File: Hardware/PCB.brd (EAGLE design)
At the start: 46 x 35 mm, 105 parts, among them IC1 DRV2605YZFR_DRV2605YZFR, IC2 BQ25180YBGR_BQ25180YBGR, IC3 BMA423_BMA423, IC9 RT6160AWSC_RT6160AWSC, J1 503480-2400_503480-2400, J2 TC2030-IDC_TC2030-IDC, J4 KH-TYPE-C-16P_KH-TYPE-C-16P, Q3 ESP32_C6_LIBRARY_6_SI1308EDL-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, U1 NORDIC_NRF_4_NRF52840_QF, U3 ESP32_C6_LIBRARY_MAX17048G+T10, X2 32.768kHz

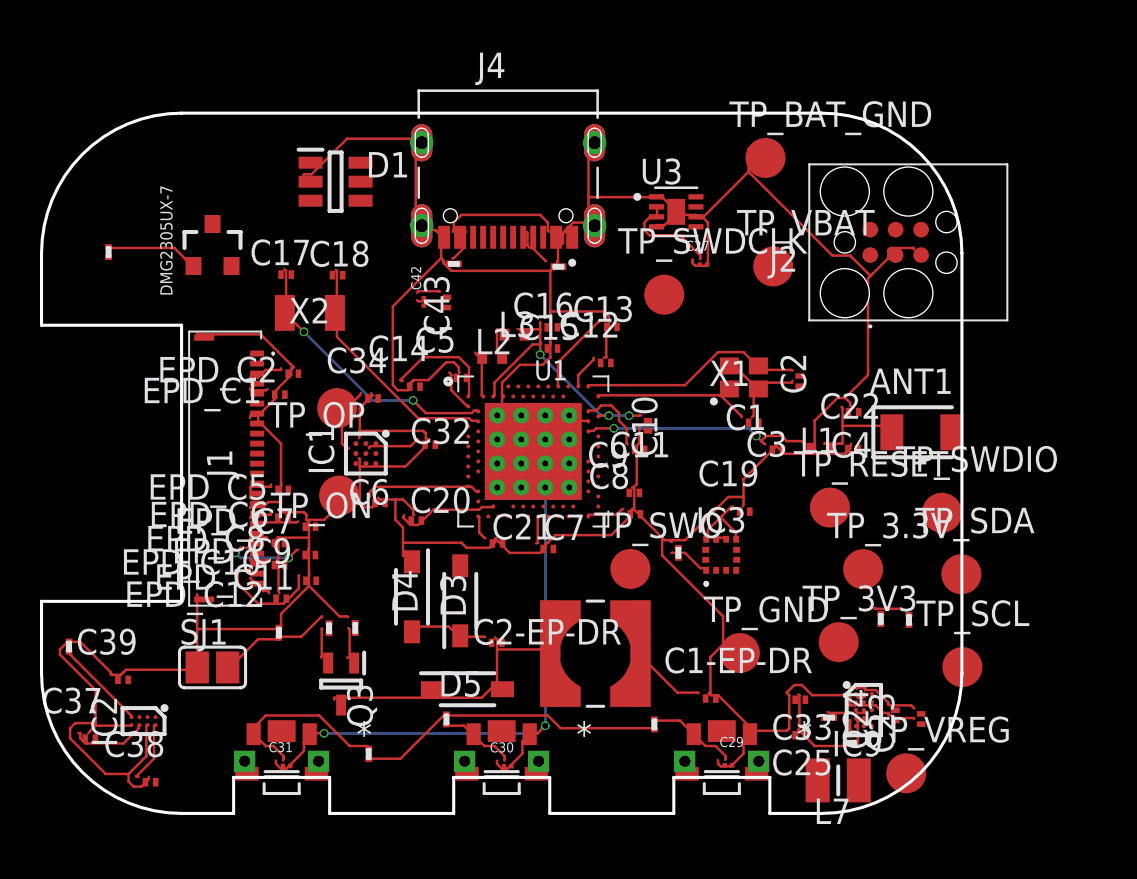
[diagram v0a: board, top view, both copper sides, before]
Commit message: Improve pcb in regards to review
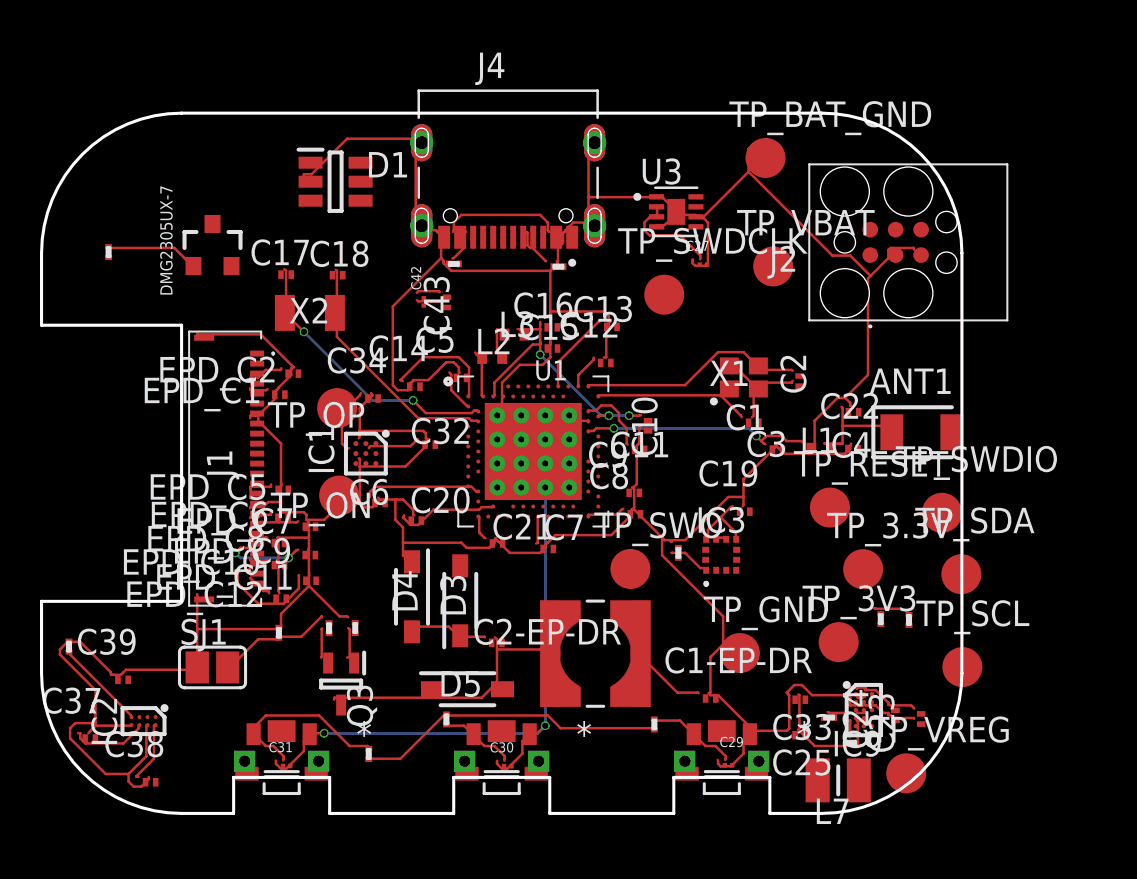
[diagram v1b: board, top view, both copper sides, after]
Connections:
- net N$127 renamed EPD_OP
- net N$128 renamed EPD_ON
- net N$13 renamed VREG
- net N$137 renamed VBAT
- net N$19 renamed I2C_SCL
- net N$20 renamed I2C_SDA
- net N$33 renamed VDD_3V3_MON
- net N$34 renamed NRST
- net N$35 renamed SWDCLK
- net N$36 renamed SWDIO
- net N$37 renamed SWO
- net N$74 renamed RF_MCU_MATCH
- net N$75 renamed RF_MATCH_ANT
- net N$9 renamed VDD_3V3
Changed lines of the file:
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@@
 <wire x1="-59.69" y1="-8.001" x2="-59.5926125" y2="-7.950528125" width="0.127" layer="1"/>
 </signal>
-<signal name="N$9">
+<signal name="VDD_3V3">
 <contactref element="TP_3V3" pad="TP"/>
 </signal>
-<signal name="N$13">
+<signal name="VREG">
 <contactref element="TP_VREG" pad="TP"/>
 </signal>
@@
 <contactref element="R18" pad="2"/>
 </signal>
-<signal name="N$19">
+<signal name="I2C_SCL">
 <contactref element="TP_SCL" pad="TP"/>
 </signal>
-<signal name="N$20">
+<signal name="I2C_SDA">
 <contactref element="TP_SDA" pad="TP"/>
 </signal>
@@
 <wire x1="-67.564" y1="-1.524" x2="-67.523490625" y2="-1.633875" width="0.127" layer="1"/>
 </signal>
-<signal name="N$33">
+<signal name="VDD_3V3_MON">
 <contactref element="TP_3.3V" pad="TP"/>
 </signal>
-<signal name="N$34">
+<signal name="NRST">
 <contactref element="TP_RESET" pad="TP"/>
 </signal>
-<signal name="N$35">
+<signal name="SWDCLK">
 <contactref element="TP_SWDCLK" pad="TP"/>
 </signal>
-<signal name="N$36">
+<signal name="SWDIO">
 <contactref element="TP_SWDIO" pad="TP"/>
 </signal>
-<signal name="N$37">
+<signal name="SWO">
 <contactref element="TP_SWO" pad="TP"/>
 </signal>
@@
 <contactref element="U1" pad="P$J24"/>
 </signal>
-<signal name="N$74">
+<signal name="RF_MCU_MATCH">
 <contactref element="U1" pad="P$H23"/>
 <contactref element="L1" pad="1"/>
@@
 </via>
 </signal>
-<signal name="N$75">
+<signal name="RF_MATCH_ANT">
 <contactref element="L1" pad="2"/>
 <contactref element="ANT1" pad="1"/>
@@
 <contactref element="R_PWR_EPD" pad="2"/>
 </signal>
-<signal name="N$127">
+<signal name="EPD_OP">
 <contactref element="TP_OP" pad="TP"/>
 </signal>
-<signal name="N$128">
+<signal name="EPD_ON">
 <contactref element="TP_ON" pad="TP"/>
 </signal>
@@
 <wire x1="-80.391" y1="-8.89" x2="-80.506025" y2="-8.810565625" width="0.127" layer="1"/>
 </signal>
-<signal name="N$137">
+<signal name="VBAT">
 <contactref element="TP_VBAT" pad="TP"/>
 </signal>
